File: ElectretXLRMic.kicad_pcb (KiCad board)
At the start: 2 copper layers, 37 x 52 mm, 38 parts, among them IC1 OPA1678IDR, J1 MIC, J2 XLR3

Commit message: Small changes to the layout
[KiCad Version: 9.0.7]
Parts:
- moved R4 0.42 mm to (107.0, 93.6)
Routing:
- net V-: track 6.13 -> 6.12 mm, vias 234 -> 225

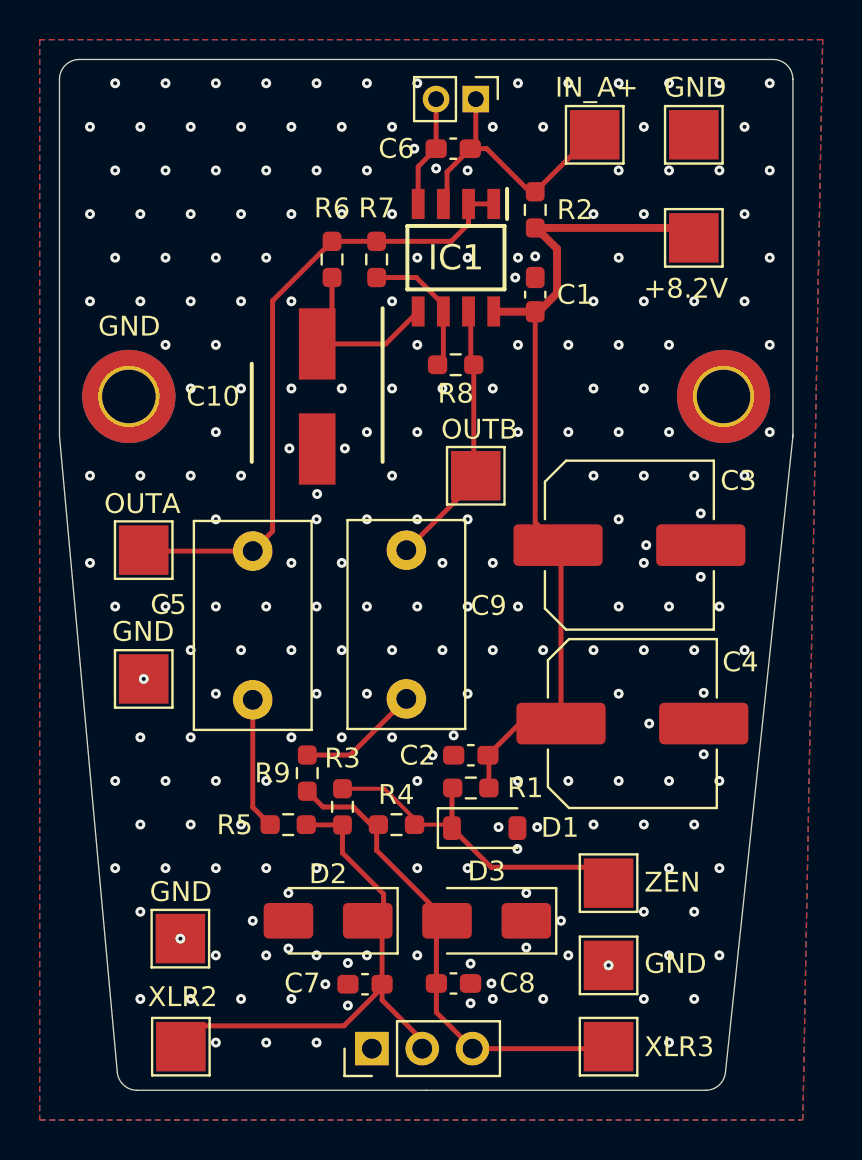
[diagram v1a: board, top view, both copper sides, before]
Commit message: Test of the circuit is done and final adjustments done for values. BOM has reduced amount of resistors and capacitors. Added 2.54 mm pitch wire terminals to BOM because getting the wires to the connectors was a pain.
[KiCad Version: 9.0.7]
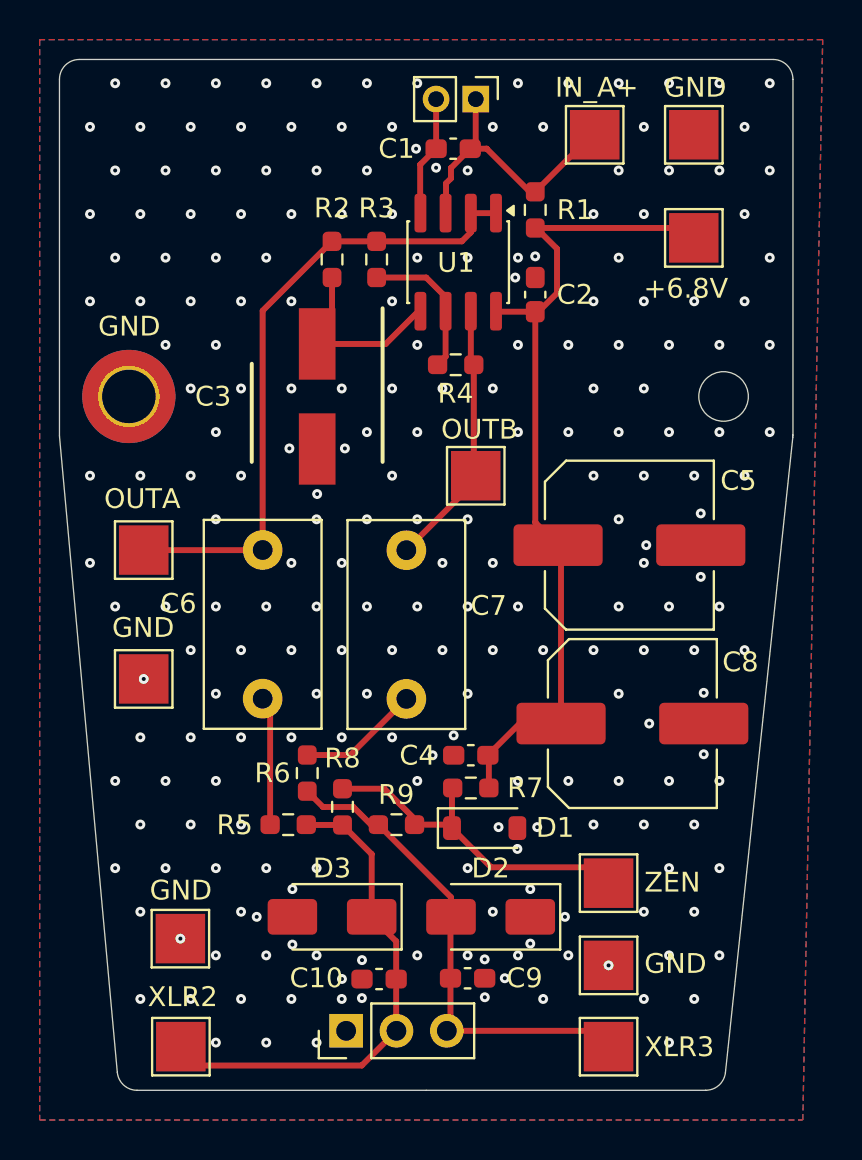
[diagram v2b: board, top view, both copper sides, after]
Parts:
- removed IC1: OPA1678IDR, SamacSys_Parts:SOIC127P600X175-8N
- added U1: OPA1678, Package_SO:SOIC-8_3.9x4.9mm_P1.27mm, F.Cu at (110.1, 65.2)
- H1: value MountingHole_Pad -> MountingHole_GND
- H2: value MountingHole_Pad -> MountingHole; footprint MountingHole:MountingHole_2.7mm_M2.5_DIN965_Pad_TopBottom -> MountingHole:MountingHole_2.5mm
- R1: renamed from R2; value 6.8k -> 7.5k
- moved J2 1.58 mm to (104.5, 104.0)
- moved C10 0.76 mm to (106.1, 101.4)
- moved C9 0.76 mm to (110.6, 101.3)
- moved C6 0.50 mm to (100.2, 87.2)
- moved D2 0.28 mm to (111.8, 98.2)
- moved D3 0.28 mm to (103.8, 98.2)
- renumbered C6 to C1, C7 to C10, C1 to C2, C10 to C3, C2 to C4, C3 to C5, C5 to C6, C9 to C7, C4 to C8, C8 to C9, D3 to D2, D2 to D3, R6 to R2, R7 to R3, R8 to R4, R9 to R6, R1 to R7, R3 to R8, R4 to R9, TP7 to TP1, TP5 to TP10, TP6 to TP11, TP1 to TP2, TP8 to TP3, TP10 to TP4, TP2 to TP5, TP3 to TP6, TP9 to TP7, TP11 to TP8, TP4 to TP9
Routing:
- net Net-(D3-A1): track 27.0 -> 25.3 mm
- net -IN_A: track 33.6 -> 32.5 mm
- net V-: track 6.12 -> 6.09 mm, vias 225 -> 229
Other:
- board text added: "+6.8V"
- board text added: "The Phantom of the Op-Amp 25.3.2026 M.H."
- board text removed: "+8.2V"
- board text removed: "The Phantom of the Op-Amp 17.3.2026 M.H."

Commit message: Added teardrops, made board slightly smaller and moved screw holes downwards.
[KiCad Version: 10.0.1]
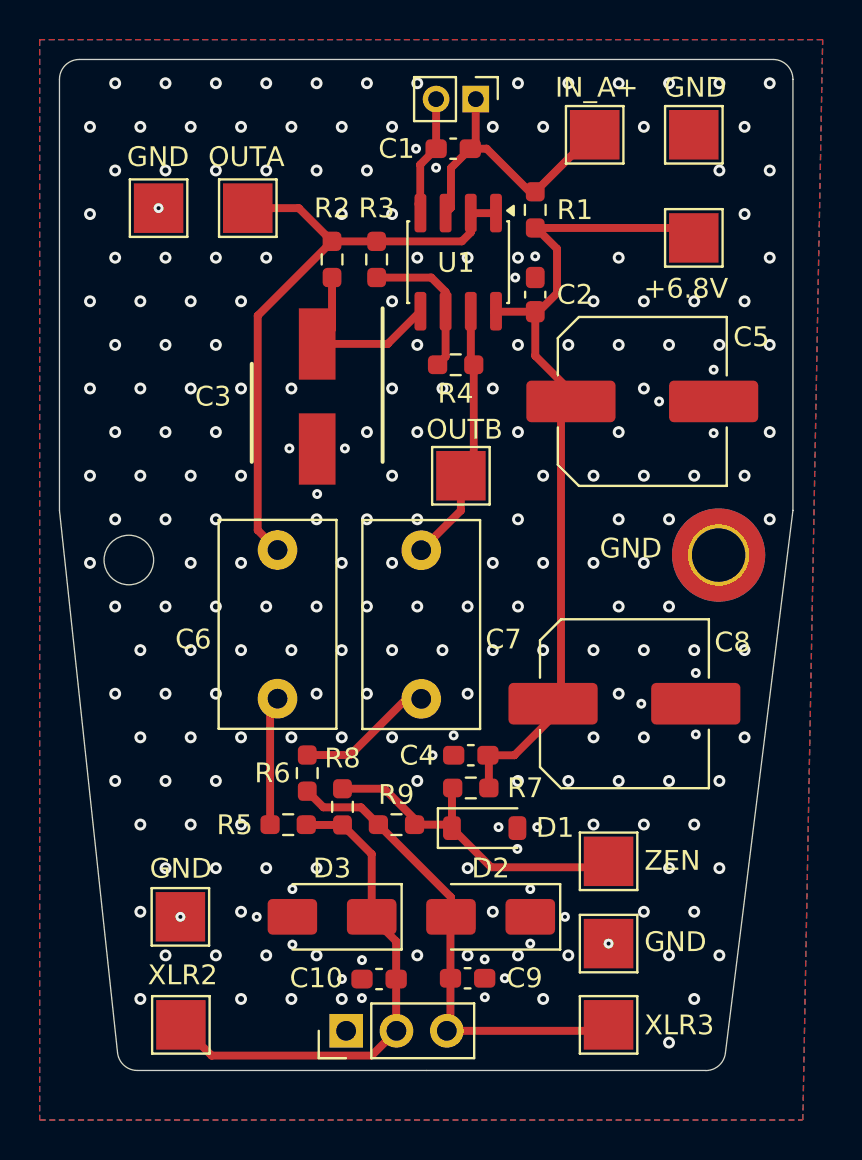
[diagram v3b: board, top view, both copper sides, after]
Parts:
- moved H2 31.1 mm to (93.5, 80.2)
- moved H1 30.8 mm to (123.2, 80.0)
- moved TP10 23.8 mm to (95.0, 62.5)
- moved TP3 18.0 mm to (99.5, 62.5)
- moved C5 7.28 mm to (119.4, 72.2)
- moved TP6 1.10 mm to (117.7, 99.6)
- moved TP11 1.10 mm to (96.1, 98.2)
- moved TP5 1.10 mm to (117.7, 95.5)
- moved TP7 1.10 mm to (96.1, 103.7)
- moved TP8 1.10 mm to (117.7, 103.7)
- moved C8 1.08 mm to (118.5, 87.5)
- moved C6 0.75 mm to (101.0, 87.2)
- moved C7 0.75 mm to (108.2, 79.8)
- moved TP4 0.75 mm to (110.2, 76.0)
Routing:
- net Net-(D2-A2): track 24.9 -> 23.4 mm
- net Net-(D1-K): track 17.6 -> 16.2 mm
- net V+: track 42.9 -> 41.6 mm
- net OUT_B: track 13.6 -> 12.9 mm
- net -IN_A: track 32.5 -> 31.9 mm
- net Net-(C6-Pad1): track 6.51 -> 5.98 mm
- net V-: track 6.09 -> 5.66 mm, vias 229 -> 227
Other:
- board size 37 x 52 mm -> 37 x 51 mm
- board text added: "The Phantom of the Op-Amp 16.4.2026 M.H."
- board text removed: "The Phantom of the Op-Amp 25.3.2026 M.H."
